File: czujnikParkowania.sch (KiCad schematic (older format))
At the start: 42 parts, among them J1 Screw_Terminal_01x03, Q1 BC817, Q2 IRF7404, Q3 BC817, Q4 BC817, Q5 BC817, U1 DC56-11SEKWA, U2 LM7805_TO220, U3 HC-SR04, U4 ATmega328-AU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

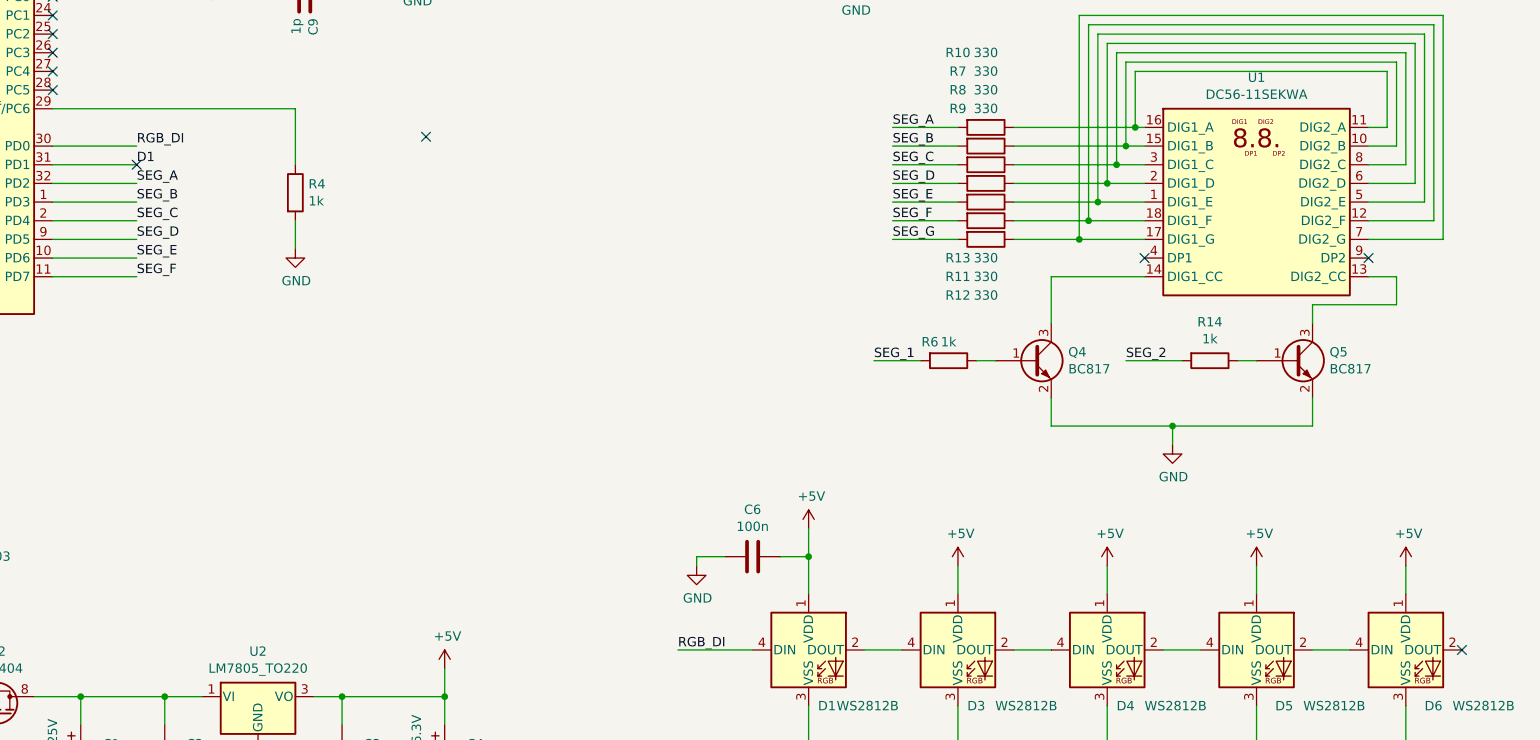
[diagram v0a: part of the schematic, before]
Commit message: added caps and button
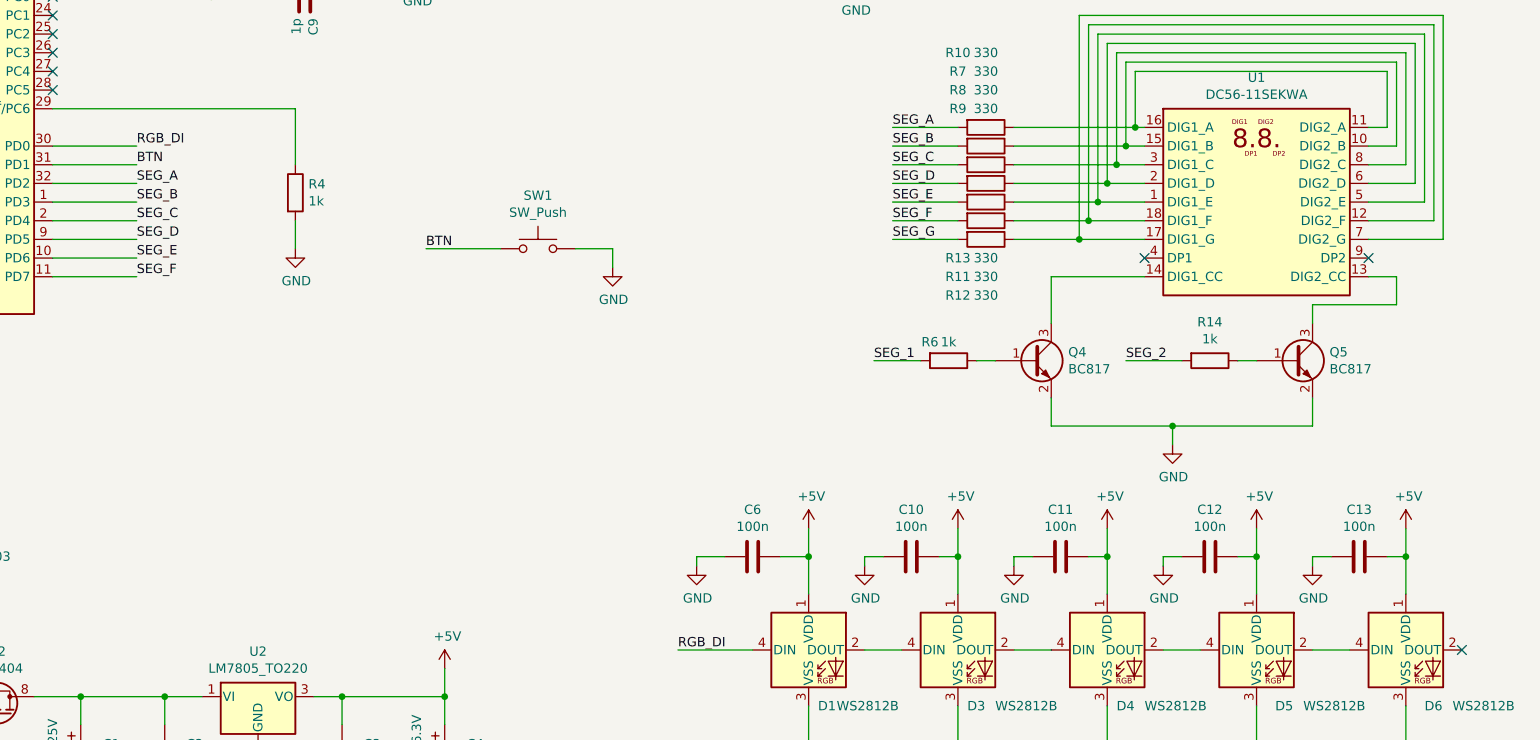
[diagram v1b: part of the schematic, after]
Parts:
- added C10, C11, C12, C13: 100n, Capacitor_SMD:C_0805_2012Metric, symbol Device:C
- added SW1: SW_Push, Button_Switch_SMD:SW_SPST_B3S-1000, symbol Switch:SW_Push
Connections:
- net +5V: now also C10.1, C11.1, C12.1, C13.1
- net GND: now also C10.2, C11.2, C12.2, C13.2, SW1.2
- net D1 renamed BTN
- net BTN: now also SW1.1
- no-connect marks 13 -> 11
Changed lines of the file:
@@
 L power:+5V #PWR0121
 U 1 1 5EB28EBD
-P 7550 5200
-F 0 "#PWR0121" H 7550 5050 50  0001 C CNN
-F 1 "+5V" H 7565 5373 50  0000 C CNN
-F 2 "" H 7550 5200 50  0001 C CNN
-F 3 "" H 7550 5200 50  0001 C CNN
-	1    7550 5200
+P 7550 5000
+F 0 "#PWR0121" H 7550 4850 50  0001 C CNN
+F 1 "+5V" H 7565 5173 50  0000 C CNN
+F 2 "" H 7550 5000 50  0001 C CNN
+F 3 "" H 7550 5000 50  0001 C CNN
+	1    7550 5000
 	1    0    0    -1
 $EndComp
@@
 L power:+5V #PWR0122
 U 1 1 5EB296B5
-P 8350 5200
-F 0 "#PWR0122" H 8350 5050 50  0001 C CNN
-F 1 "+5V" H 8365 5373 50  0000 C CNN
-F 2 "" H 8350 5200 50  0001 C CNN
-F 3 "" H 8350 5200 50  0001 C CNN
-	1    8350 5200
+P 8350 5000
+F 0 "#PWR0122" H 8350 4850 50  0001 C CNN
+F 1 "+5V" H 8365 5173 50  0000 C CNN
+F 2 "" H 8350 5000 50  0001 C CNN
+F 3 "" H 8350 5000 50  0001 C CNN
+	1    8350 5000
 	1    0    0    -1
 $EndComp
@@
 L power:+5V #PWR0123
 U 1 1 5EB2995A
-P 9150 5200
-F 0 "#PWR0123" H 9150 5050 50  0001 C CNN
-F 1 "+5V" H 9165 5373 50  0000 C CNN
-F 2 "" H 9150 5200 50  0001 C CNN
-F 3 "" H 9150 5200 50  0001 C CNN
-	1    9150 5200
+P 9150 5000
+F 0 "#PWR0123" H 9150 4850 50  0001 C CNN
+F 1 "+5V" H 9165 5173 50  0000 C CNN
+F 2 "" H 9150 5000 50  0001 C CNN
+F 3 "" H 9150 5000 50  0001 C CNN
+	1    9150 5000
 	1    0    0    -1
 $EndComp
@@
 L power:+5V #PWR0124
 U 1 1 5EB29CCE
-P 9950 5200
-F 0 "#PWR0124" H 9950 5050 50  0001 C CNN
-F 1 "+5V" H 9965 5373 50  0000 C CNN
-F 2 "" H 9950 5200 50  0001 C CNN
-F 3 "" H 9950 5200 50  0001 C CNN
-	1    9950 5200
-	1    0    0    -1
-$EndComp
-Wire Wire Line
-	7550 5200 7550 5350
-Wire Wire Line
-	8350 5200 8350 5350
-Wire Wire Line
-	9150 5200 9150 5350
-Wire Wire Line
-	9950 5200 9950 5350
+P 9950 5000
+F 0 "#PWR0124" H 9950 4850 50  0001 C CNN
+F 1 "+5V" H 9965 5173 50  0000 C CNN
+F 2 "" H 9950 5000 50  0001 C CNN
+F 3 "" H 9950 5000 50  0001 C CNN
+	1    9950 5000
+	1    0    0    -1
+$EndComp
 Wire Wire Line
 	7050 5650 7250 5650
@@
 RGB_DI
 Text Label 3150 3050 0    50   ~ 0
-D1
+BTN
 Text Label 3150 3150 0    50   ~ 0
 SEG_A
@@
 Text Label 3100 1750 0    50   ~ 0
 BUZZER
-NoConn ~ 3150 3050
-NoConn ~ 4700 2900
+$Comp
+L Switch:SW_Push SW1
+U 1 1 5EB03A69
+P 5300 3500
+F 0 "SW1" H 5300 3785 50  0000 C CNN
+F 1 "SW_Push" H 5300 3694 50  0000 C CNN
+F 2 "Button_Switch_SMD:SW_SPST_B3S-1000" H 5300 3700 50  0001 C CNN
+F 3 "https://www.tme.eu/pl/details/b3s-1000/mikroprzelaczniki-tact/omron-ocb/" H 5300 3700 50  0001 C CNN
+	1    5300 3500
+	1    0    0    -1
+$EndComp
+$Comp
+L power:GND #PWR0107
+U 1 1 5EB04454
+P 5700 3600
+F 0 "#PWR0107" H 5700 3350 50  0001 C CNN
+F 1 "GND" H 5705 3427 50  0000 C CNN
+F 2 "" H 5700 3600 50  0001 C CNN
+F 3 "" H 5700 3600 50  0001 C CNN
+	1    5700 3600
+	1    0    0    -1
+$EndComp
+Wire Wire Line
+	5700 3600 5700 3500
+Wire Wire Line
+	5700 3500 5500 3500
+Wire Wire Line
+	5100 3500 4700 3500
+Text Label 4700 3500 0    50   ~ 0
+BTN
+Wire Wire Line
+	7550 5000 7550 5150
+Wire Wire Line
+	8350 5000 8350 5150
+Wire Wire Line
+	9150 5000 9150 5150
+Wire Wire Line
+	9950 5000 9950 5150
+$Comp
+L Device:C C10
+U 1 1 5EB4CD5B
+P 7300 5150
+F 0 "C10" V 7048 5150 50  0000 C CNN
+F 1 "100n" V 7139 5150 50  0000 C CNN
+F 2 "Capacitor_SMD:C_0805_2012Metric" H 7338 5000 50  0001 C CNN
+F 3 "~" H 7300 5150 50  0001 C CNN
+	1    7300 5150
+	0    1    1    0
+$EndComp
+$Comp
+L Device:C C11
+U 1 1 5EB4D399
+P 8100 5150
+F 0 "C11" V 7848 5150 50  0000 C CNN
+F 1 "100n" V 7939 5150 50  0000 C CNN
+F 2 "Capacitor_SMD:C_0805_2012Metric" H 8138 5000 50  0001 C CNN
+F 3 "~" H 8100 5150 50  0001 C CNN
+	1    8100 5150
+	0    1    1    0
+$EndComp
+$Comp
+L Device:C C12
+U 1 1 5EB4D832
+P 8900 5150
+F 0 "C12" V 8648 5150 50  0000 C CNN
+F 1 "100n" V 8739 5150 50  0000 C CNN
+F 2 "Capacitor_SMD:C_0805_2012Metric" H 8938 5000 50  0001 C CNN
+F 3 "~" H 8900 5150 50  0001 C CNN
+	1    8900 5150
+	0    1    1    0
+$EndComp
+$Comp
+L Device:C C13
+U 1 1 5EB4DC0C
+P 9700 5150
+F 0 "C13" V 9448 5150 50  0000 C CNN
+F 1 "100n" V 9539 5150 50  0000 C CNN
+F 2 "Capacitor_SMD:C_0805_2012Metric" H 9738 5000 50  0001 C CNN
+F 3 "~" H 9700 5150 50  0001 C CNN
+	1    9700 5150
+	0    1    1    0
+$EndComp
+$Comp
+L power:GND #PWR0128
+U 1 1 5EB4DF92
+P 7050 5200
+F 0 "#PWR0128" H 7050 4950 50  0001 C CNN
+F 1 "GND" H 7055 5027 50  0000 C CNN
+F 2 "" H 7050 5200 50  0001 C CNN
+F 3 "" H 7050 5200 50  0001 C CNN
+	1    7050 5200
+	1    0    0    -1
+$EndComp
+$Comp
+L power:GND #PWR0129
+U 1 1 5EB4E269
+P 7850 5200
+F 0 "#PWR0129" H 7850 4950 50  0001 C CNN
+F 1 "GND" H 7855 5027 50  0000 C CNN
+F 2 "" H 7850 5200 50  0001 C CNN
+F 3 "" H 7850 5200 50  0001 C CNN
+	1    7850 5200
+	1    0    0    -1
+$EndComp
+$Comp
+L power:GND #PWR0130
+U 1 1 5EB4E583
+P 8650 5200
+F 0 "#PWR0130" H 8650 4950 50  0001 C CNN
+F 1 "GND" H 8655 5027 50  0000 C CNN
+F 2 "" H 8650 5200 50  0001 C CNN
+F 3 "" H 8650 5200 50  0001 C CNN
+	1    8650 5200
+	1    0    0    -1
+$EndComp
+$Comp
+L power:GND #PWR0131
+U 1 1 5EB4E84C
+P 9450 5200
+F 0 "#PWR0131" H 9450 4950 50  0001 C CNN
+F 1 "GND" H 9455 5027 50  0000 C CNN
+F 2 "" H 9450 5200 50  0001 C CNN
+F 3 "" H 9450 5200 50  0001 C CNN
+	1    9450 5200
+	1    0    0    -1
+$EndComp
+Wire Wire Line
+	7150 5150 7050 5150
+Wire Wire Line
+	7050 5150 7050 5200
+Wire Wire Line
+	7450 5150 7550 5150
+Connection ~ 7550 5150
+Wire Wire Line
+	7550 5150 7550 5350
+Wire Wire Line
+	7950 5150 7850 5150
+Wire Wire Line
+	7850 5150 7850 5200
+Wire Wire Line
+	8250 5150 8350 5150
+Connection ~ 8350 5150
+Wire Wire Line
+	8350 5150 8350 5350
+Wire Wire Line
+	8750 5150 8650 5150
+Wire Wire Line
+	8650 5150 8650 5200
+Wire Wire Line
+	9050 5150 9150 5150
+Connection ~ 9150 5150
+Wire Wire Line
+	9150 5150 9150 5350
+Wire Wire Line
+	9550 5150 9450 5150
+Wire Wire Line
+	9450 5150 9450 5200
+Wire Wire Line
+	9850 5150 9950 5150
+Connection ~ 9950 5150
+Wire Wire Line
+	9950 5150 9950 5350
 $EndSCHEMATC

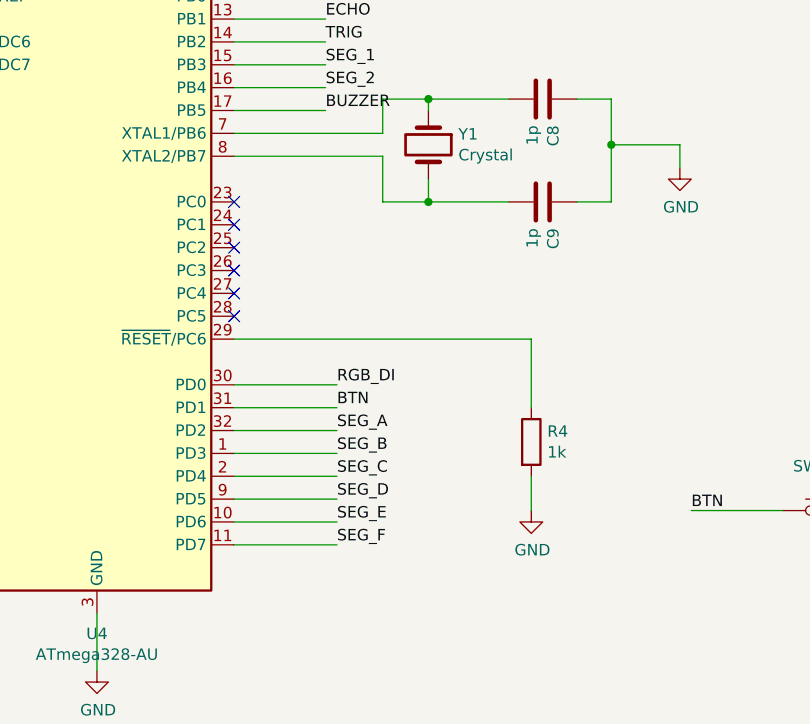
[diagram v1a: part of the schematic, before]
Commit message: schematic reset pin bugfix
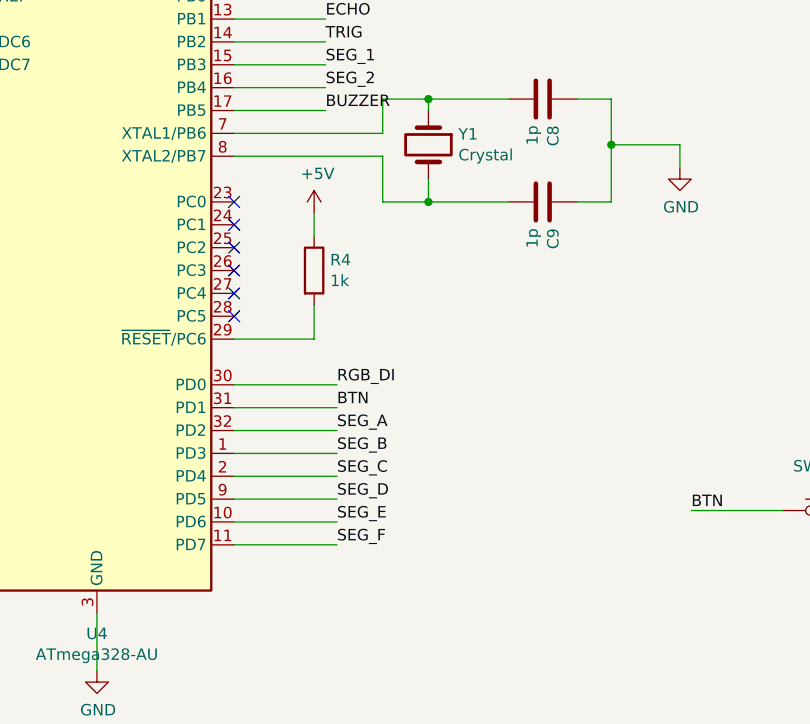
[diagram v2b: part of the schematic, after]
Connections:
- net +5V: now also R4.1
- net GND: no longer R4.2
- net at U4.29 (~RESET~/PC6): now also R4.2; no longer R4.1
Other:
- moved on the sheet: R4
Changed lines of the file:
@@
 Wire Wire Line
 	2700 3650 3150 3650
-Wire Wire Line
-	2700 2750 4000 2750
-$Comp
-L power:GND #PWR0127
-U 1 1 5EBE9E5B
-P 4000 3500
-F 0 "#PWR0127" H 4000 3250 50  0001 C CNN
-F 1 "GND" H 4005 3327 50  0000 C CNN
-F 2 "" H 4000 3500 50  0001 C CNN
-F 3 "" H 4000 3500 50  0001 C CNN
-	1    4000 3500
-	1    0    0    -1
-$EndComp
 $Comp
 L Device:R R4
 U 1 1 5EBEA221
-P 4000 3200
-F 0 "R4" H 4070 3246 50  0000 L CNN
-F 1 "1k" H 4070 3155 50  0000 L CNN
-F 2 "Resistor_SMD:R_0805_2012Metric" V 3930 3200 50  0001 C CNN
-F 3 "~" H 4000 3200 50  0001 C CNN
-	1    4000 3200
-	1    0    0    -1
-$EndComp
-Wire Wire Line
-	4000 2750 4000 3050
-Wire Wire Line
-	4000 3350 4000 3500
+P 3050 2450
+F 0 "R4" H 3120 2496 50  0000 L CNN
+F 1 "1k" H 3120 2405 50  0000 L CNN
+F 2 "Resistor_SMD:R_0805_2012Metric" V 2980 2450 50  0001 C CNN
+F 3 "~" H 3050 2450 50  0001 C CNN
+	1    3050 2450
+	1    0    0    -1
+$EndComp
 NoConn ~ 1500 1450
 NoConn ~ 1500 1550
@@
 Wire Wire Line
 	9950 5150 9950 5350
+Wire Wire Line
+	2700 2750 3050 2750
+Wire Wire Line
+	3050 2750 3050 2600
+$Comp
+L power:+5V #PWR?
+U 1 1 5EADD758
+P 3050 2200
+F 0 "#PWR?" H 3050 2050 50  0001 C CNN
+F 1 "+5V" H 3065 2373 50  0000 C CNN
+F 2 "" H 3050 2200 50  0001 C CNN
+F 3 "" H 3050 2200 50  0001 C CNN
+	1    3050 2200
+	1    0    0    -1
+$EndComp
+Wire Wire Line
+	3050 2200 3050 2300
 $EndSCHEMATC
